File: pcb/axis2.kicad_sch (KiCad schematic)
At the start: 7 parts, among them J12 Mini v1.0 / 15-hole socket, J22 MOTOR PHASES male 1x3, J32 ENCODER breakout FEMALE 1x6

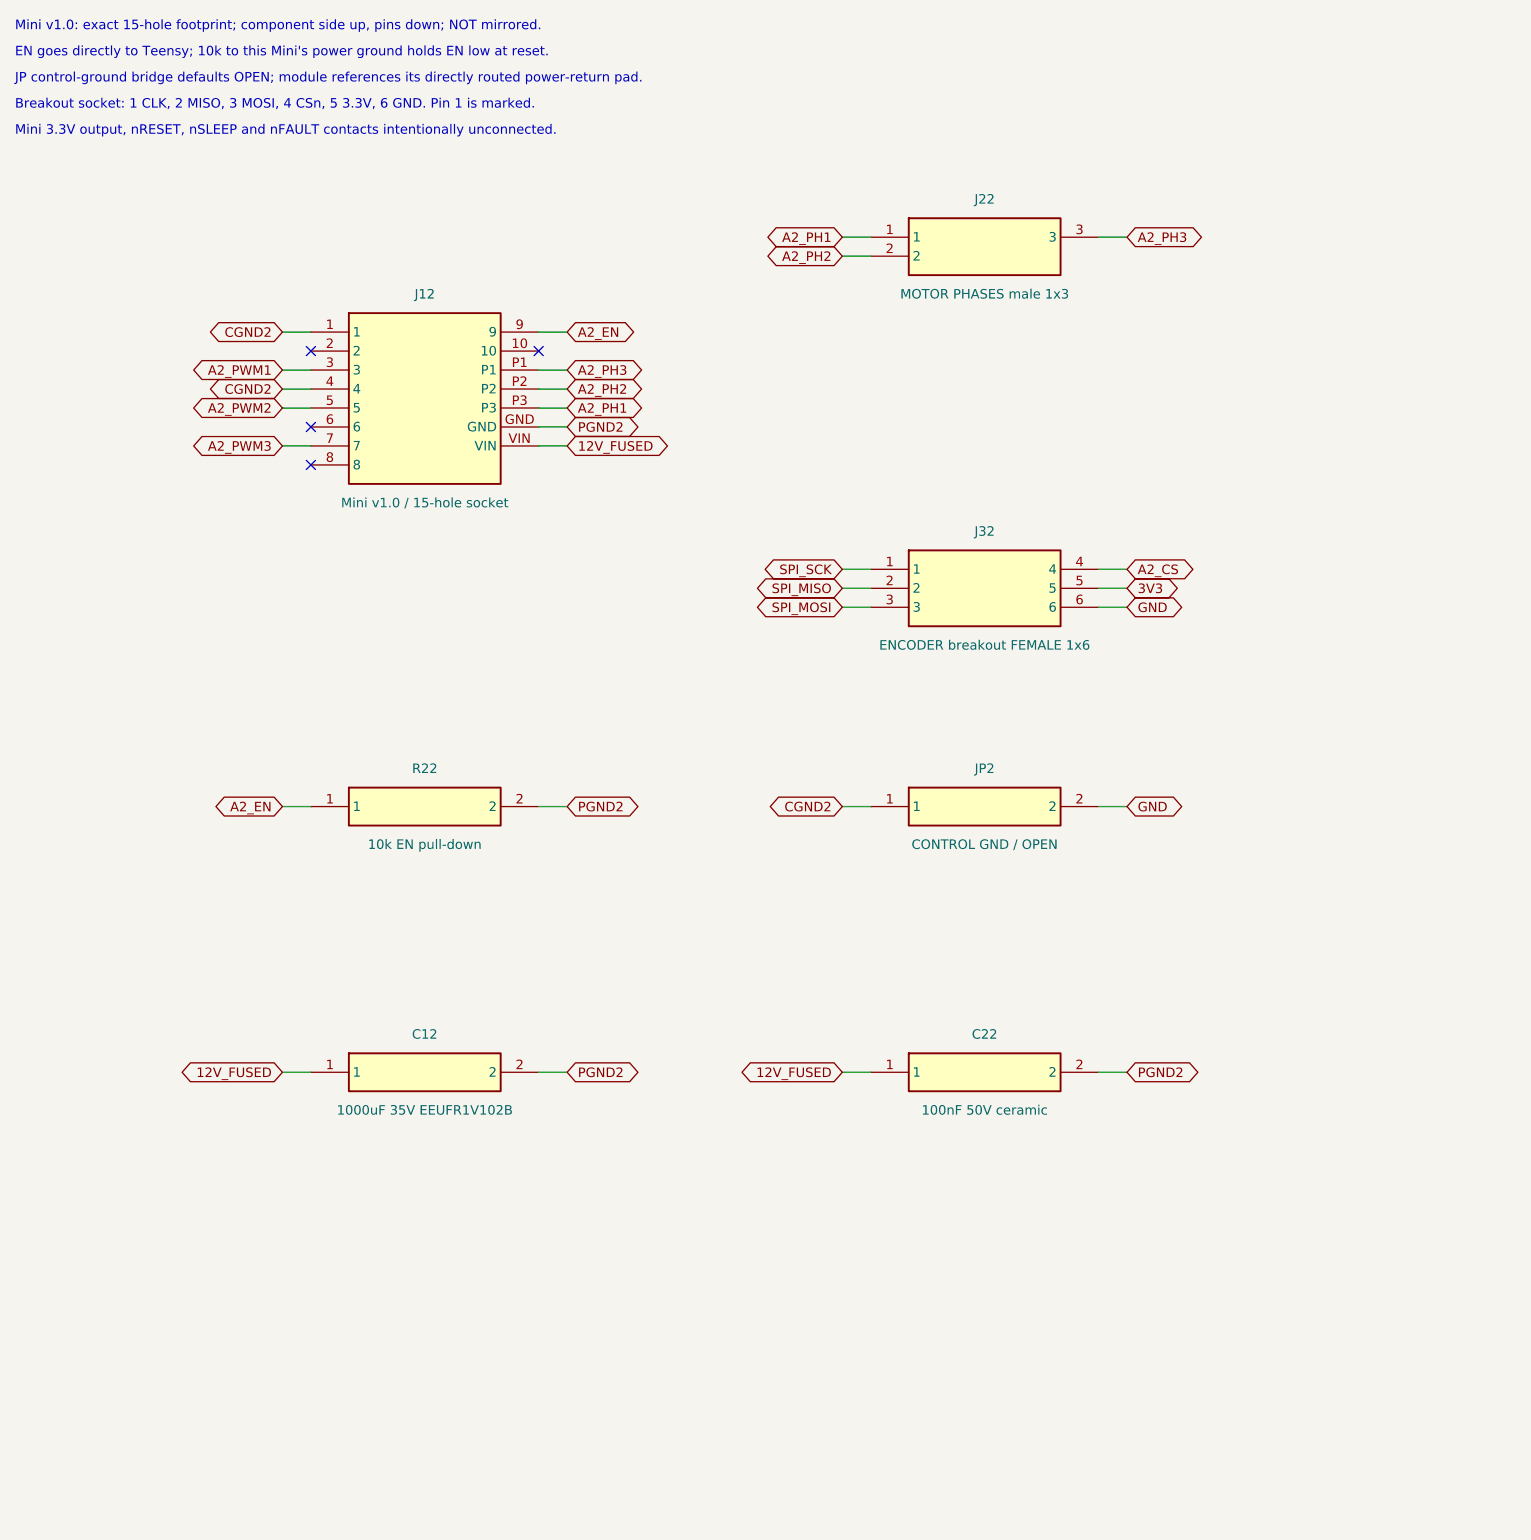
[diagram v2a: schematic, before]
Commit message: feat: relayout carrier with edge connectors and hardware kill
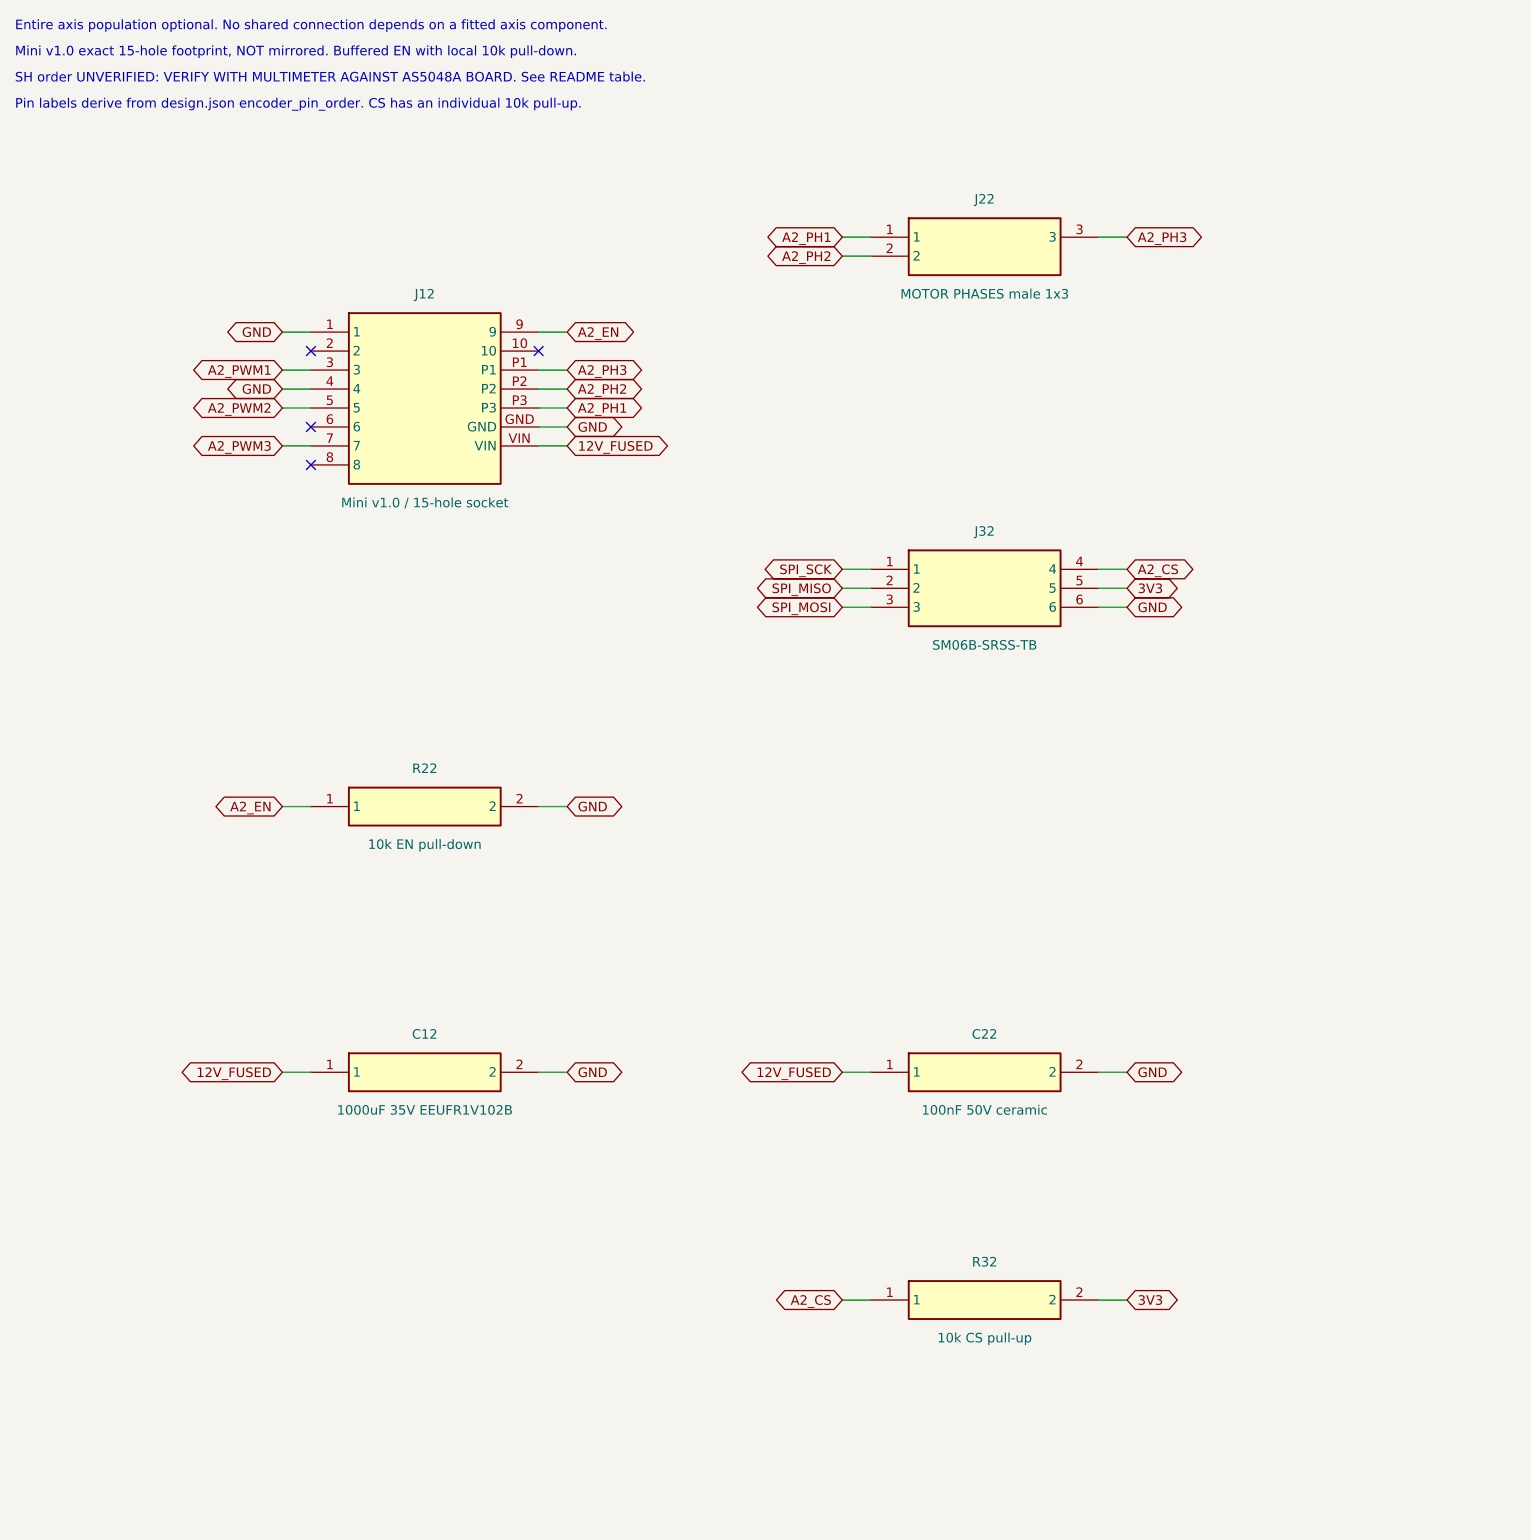
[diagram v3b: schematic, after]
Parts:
- removed JP2: CONTROL GND / OPEN, TrueSkate:GroundBridge_THT, symbol TrueSkate:JP2
- added R32: 10k CS pull-up, TrueSkate:Edge_R_Axial_DIN0207_L6.3mm_D2.5mm_P7.62mm_Horizontal, symbol TrueSkate:R32
- C12: footprint Capacitor_THT:CP_Radial_D12.5mm_P5.00mm -> TrueSkate:Edge_CP_Radial_D12.5mm_P5.00mm
- C22: footprint Capacitor_THT:C_Disc_D5.0mm_W2.5mm_P5.00mm -> TrueSkate:Edge_C_Disc_D5.0mm_W2.5mm_P5.00mm
- J22: footprint Connector_PinHeader_2.54mm:PinHeader_1x03_P2.54mm_Vertical -> TrueSkate:Edge_PinHeader_1x03_P2.54mm_Vertical
- J32: value ENCODER breakout FEMALE 1x6 -> SM06B-SRSS-TB; footprint Connector_PinSocket_2.54mm:PinSocket_1x06_P2.54mm_Vertical -> TrueSkate:Edge_JST_SH_SM06B-SRSS-TB_1x06-1MP_P1.00mm_Horizontal
- R22: footprint Resistor_THT:R_Axial_DIN0207_L6.3mm_D2.5mm_P7.62mm_Horizontal -> TrueSkate:Edge_R_Axial_DIN0207_L6.3mm_D2.5mm_P7.62mm_Horizontal
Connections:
- net CGND2 is gone; now on net GND: J12.1, J12.4
- net PGND2 is gone; now on net GND: C12.2, C22.2, J12.GND, R22.2
- net 3V3: now also R32.2
- net A2_CS: now also R32.1
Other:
- note added: "Entire axis population optional. No shared connection depends on a fitted axis component."
- note added: "Mini v1.0 exact 15-hole footprint, NOT mirrored. Buffered EN with local 10k pull-down."
- note added: "Pin labels derive from design.json encoder_pin_order. CS has an individual 10k pull-up."
- note added: "SH order UNVERIFIED: VERIFY WITH MULTIMETER AGAINST AS5048A BOARD. See README table."
- note removed: "Breakout socket: 1 CLK, 2 MISO, 3 MOSI, 4 CSn, 5 3.3V, 6 GND. Pin 1 is marked."
- note removed: "EN goes directly to Teensy; 10k to this Mini's power ground holds EN low at reset."
- note removed: "JP control-ground bridge defaults OPEN; module references its directly routed power-return pad."
- note removed: "Mini 3.3V output, nRESET, nSLEEP and nFAULT contacts intentionally unconnected."
- note removed: "Mini v1.0: exact 15-hole footprint; component side up, pins down; NOT mirrored."
